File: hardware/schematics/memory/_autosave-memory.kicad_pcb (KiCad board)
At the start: 2 copper layers, 74.9 x 58.4 mm, 5 parts, among them J1 Conn_02x20_Counter_Clockwise, U1 28C256, U2 HM62256BLP

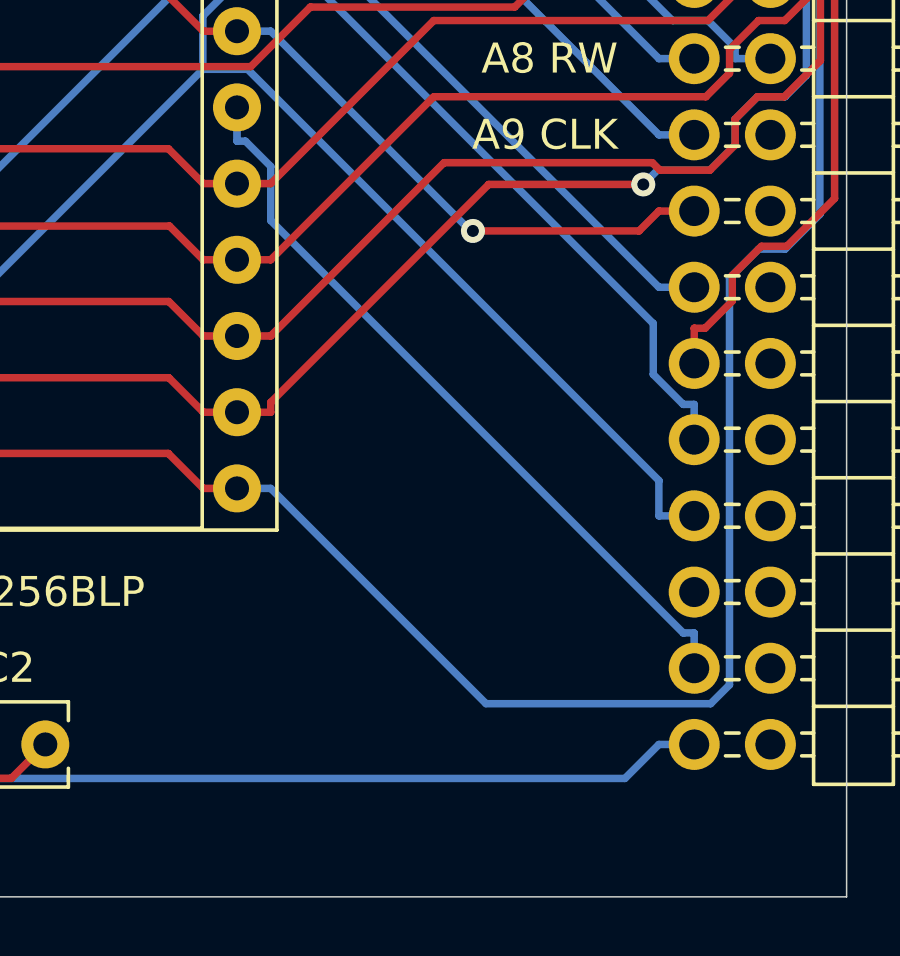
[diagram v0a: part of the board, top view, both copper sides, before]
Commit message: I ordered the PCB from jlcpcb
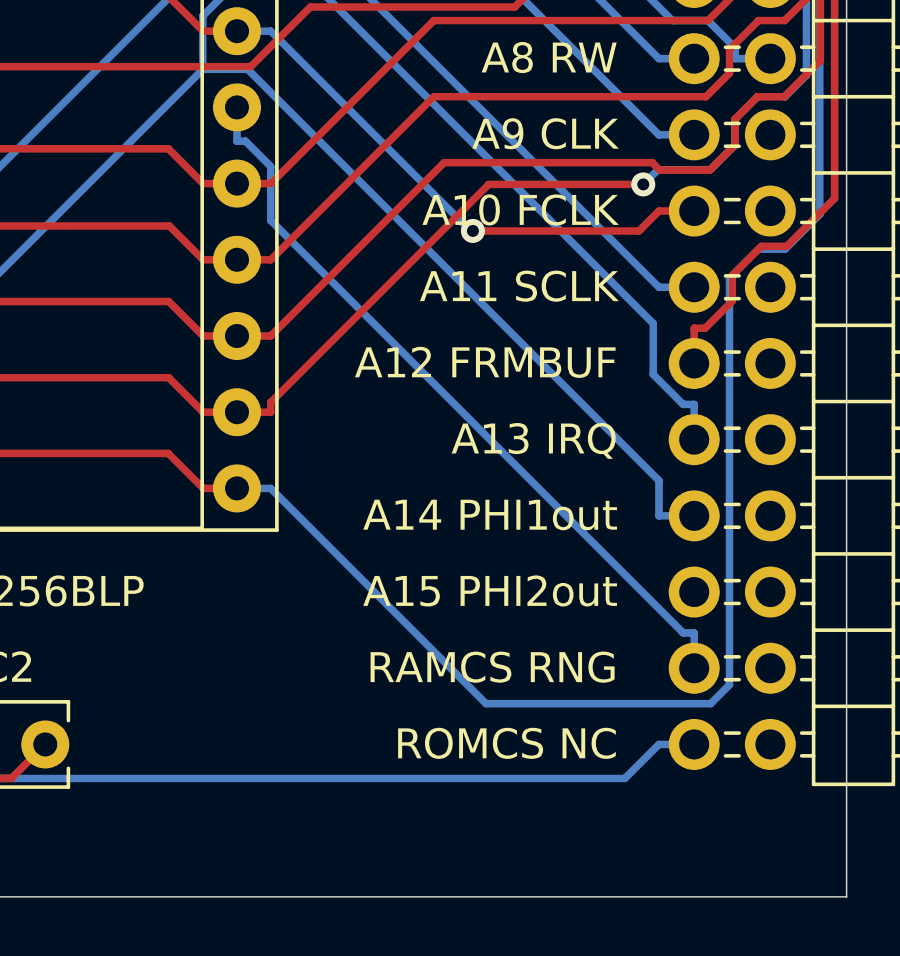
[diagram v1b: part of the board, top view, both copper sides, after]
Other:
- board text added: "A10 FCLK"
- board text added: "A11 SCLK"
- board text added: "A12 FRMBUF"
- board text added: "A13 IRQ"
- board text added: "A14 PHI1out"
- board text added: "A15 PHI2out"
- board text added: "RAMCS RNG"
- board text added: "ROMCS NC"
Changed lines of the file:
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@@
   (general
     (thickness 1.6)
-    (drawings 19)
+    (drawings 27)
     (tracks 442)
     (zones 0)
@@
     (pcbplotparams
       (layerselection 0x010fc_ffffffff)
-      (usegerberextensions false)
-      (usegerberattributes true)
-      (usegerberadvancedattributes true)
-      (creategerberjobfile true)
+      (usegerberextensions true)
+      (usegerberattributes false)
+      (usegerberadvancedattributes false)
+      (creategerberjobfile false)
       (excludeedgelayer true)
       (linewidth 0.100000)
@@
       (psa4output false)
       (plotreference true)
-      (plotvalue true)
+      (plotvalue false)
       (plotinvisibletext false)
       (padsonsilk false)
-      (subtractmaskfromsilk false)
+      (subtractmaskfromsilk true)
       (outputformat 1)
       (mirror false)
-      (drillshape 1)
+      (drillshape 0)
       (scaleselection 1)
       (outputdirectory ""))
@@
     )
   )
+  (gr_text "ROMCS NC" (at 172.72 95.25) (layer F.SilkS)
+    (effects (font (size 1 1) (thickness 0.15)) (justify right))
+  )
+  (gr_text "RAMCS RNG" (at 172.72 92.71) (layer F.SilkS)
+    (effects (font (size 1 1) (thickness 0.15)) (justify right))
+  )
+  (gr_text "A15 PHI2out" (at 172.72 90.17) (layer F.SilkS)
+    (effects (font (size 1 1) (thickness 0.15)) (justify right))
+  )
+  (gr_text "A14 PHI1out" (at 172.72 87.63) (layer F.SilkS)
+    (effects (font (size 1 1) (thickness 0.15)) (justify right))
+  )
+  (gr_text "A13 IRQ" (at 172.72 85.09) (layer F.SilkS)
+    (effects (font (size 1 1) (thickness 0.15)) (justify right))
+  )
+  (gr_text "A12 FRMBUF" (at 172.72 82.55) (layer F.SilkS)
+    (effects (font (size 1 1) (thickness 0.15)) (justify right))
+  )
+  (gr_text "A11 SCLK" (at 172.72 80.01) (layer F.SilkS)
+    (effects (font (size 1 1) (thickness 0.15)) (justify right))
+  )
+  (gr_text "A10 FCLK" (at 172.72 77.47) (layer F.SilkS)
+    (effects (font (size 1 1) (thickness 0.15)) (justify right))
+  )
   (gr_text "A9 CLK" (at 172.72 74.93) (layer F.SilkS)
